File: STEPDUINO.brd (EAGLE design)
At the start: 112.4 x 73.7 mm, 126 parts, among them IC1 HEF4050B, IC2 MC34063, IC3 LD111733, IC4 74HC4094, IC5 ATmega32U4, IC6 DRV8811, IC7 DRV8811, J1 SERVO, J10 Touchscreen, J11 Touchscreen, J12 X-MOTOR, J13 MS1, J14 MS0, J15 Y-MOTOR, J16 MS1, J17 MS0, J2 Z-DRIVE, J3 ISP, J4 UART, J5 12V Supply, J6 MicroSD Card, J7 HWB, J8 USB-6PSMT, J9 Home Switches, Q1 16MHz

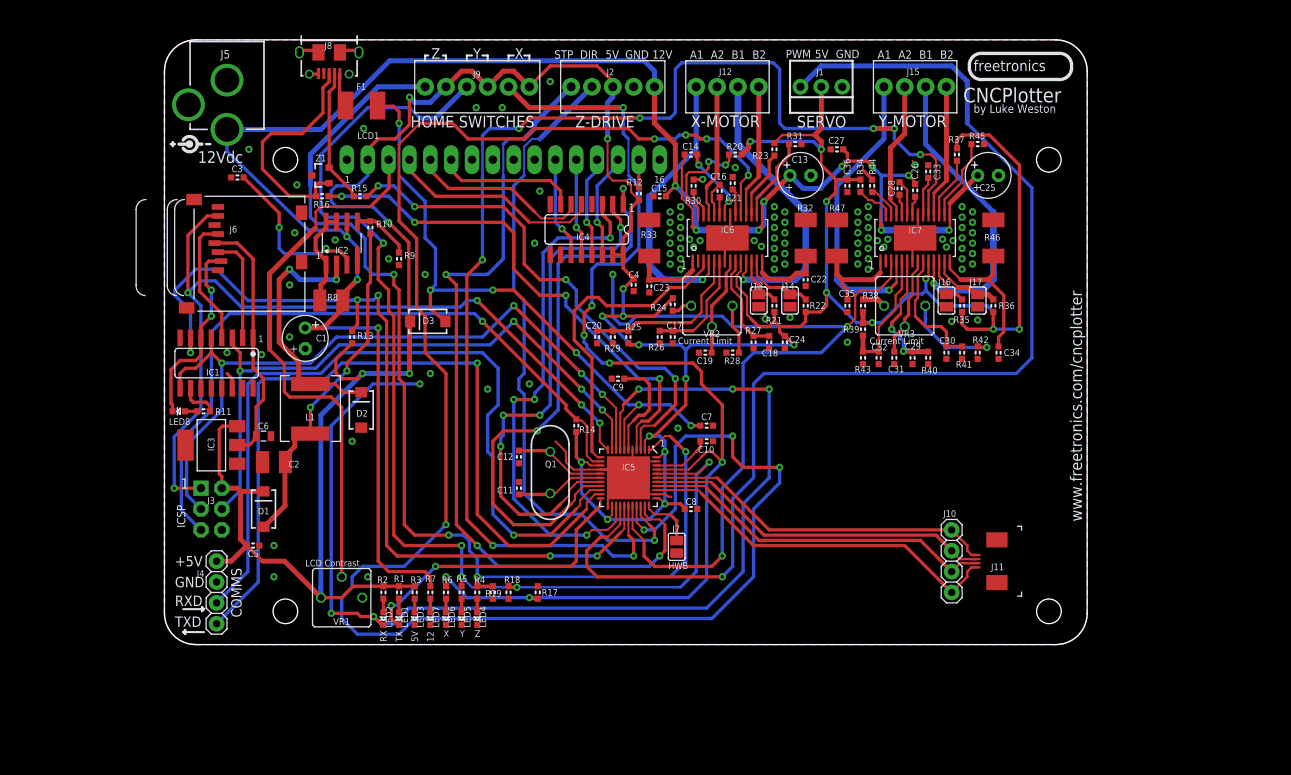
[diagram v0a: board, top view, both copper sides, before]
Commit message: Start of major restructure using ATmega328
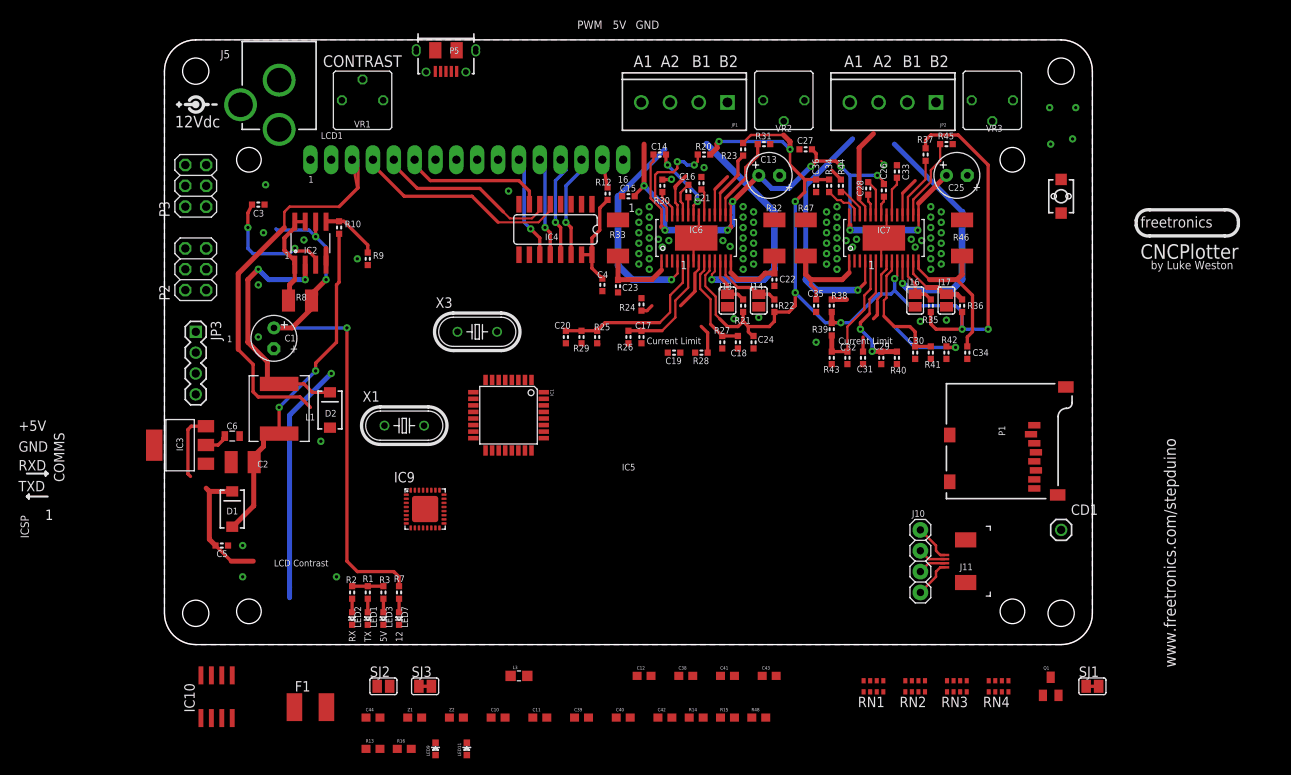
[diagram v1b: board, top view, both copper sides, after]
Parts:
- removed C7, C8: 100nF, freetronics-master-v1:0603
- removed C9: 1µF, freetronics-master-v1:0603
- removed D3: CDBA120, freetronics-luke:SMA
- removed IC5: ATmega32U4, freetronics-jon:QFN-44N
- removed J1: SERVO, con-molex:22-23-2031
- removed J12: X-MOTOR, con-phoenix-254:4POL254
- removed J15: Y-MOTOR, con-phoenix-254:4POL254
- removed J2: Z-DRIVE, con-phoenix-254:5POL254
- removed J3: ISP, SparkFun:2X3-NS
- removed J4: UART, pinhead:1X04
- removed J6: MicroSD Card, RAMPSdisplay:ADAFRUIT_MICROSD
- removed J7: HWB, freetronics-luke:SJ
- removed J8: USB-6PSMT, freetronics-jon:USB-MICROB-MB05PMXX
- removed J9: Home Switches, con-phoenix-254:6POL254
- removed LED4: Z, freetronics-master-v1:LED-0603
- removed LED5: Y, freetronics-master-v1:LED-0603
- removed LED6: X, freetronics-master-v1:LED-0603
- removed LED8: SD, freetronics-master-v1:LED-0603
- removed R11, R4, R5, R6: 1k, freetronics-master-v1:0603
- removed R17, R18, R19: 10k, freetronics-master-v1:0603
- added C38, C41, C43, C44: 100nF 0603, freetronics:0603
- added C39, C40: 22pF 0603, freetronics:0603
- added C42: 1uF 0603, freetronics:0603
- added CD1: M01PTH, freetronics-2:1X01
- added IC10: LM358D, linear:SO08
- added IC9: ATMEGA16U2-MU, freetronics-jon:ATMEL_QFN32
- added JP1, JP2: (no value), freetronics-master-v1:SCREWTERMINAL-3.5MM-4
- added JP3: (no value), freetronics-master-v1:1X04
- added L3: 0805 INDUCTOR, freetronics-master-v1:0805-LARGE
- added LED11: TX/YEL, freetronics:LED-0603
- added LED9: RX/GRN, freetronics:LED-0603
- added P1: microSD, freetronics-master-v1:MICRO-SD-SOCKET-PP
- added P2: ICSP:MAIN, pinhead:2X03
- added P3: ICSP:USB, pinhead:2X03
- added P5: USB-6PSMT, freetronics-jon:USB-MICROB-MB05PMXX
- added R48: 27R 0603, freetronics:0603
- added RN1: 2K2, freetronics-master-v1:CAY16
- added RN2, RN3: 1K, freetronics-master-v1:CAY16
- added RN4: 10K, freetronics-master-v1:CAY16
- added S7: RESET, freetronics-master-v1:TACTILE_SWITCH_SMD_2PIN_TINY
- added SJ1: GROUND, freetronics-jon:SJC
- added SJ2: UBOOT, jumper:SJ
- added SJ3: RESET-EN, freetronics-jon:SJC
- added X1, X3: 16MHz, freetronics-master-v1:HC49U-V
- added Z2: PGB1010603, freetronics:0603
- C10: value 100nF -> 22pF 0603; device freetronics-master-v1:0603 -> freetronics:0603
- C11: value 22pF -> 22pF 0603; device freetronics-master-v1:0603 -> freetronics:0603
- C12: value 22pF -> 100nF 0603; device freetronics-master-v1:0603 -> freetronics:0603
- F1: value 500mA -> 500mA PTC 1812; device freetronics-luke:1812 -> rcl:L1812
- IC1: value HEF4050B -> ATMEGA328P TQFP32; device 40xx:SO16 -> freetronics-2:TQFP32-08
- IC3: value LD111733 -> LD111733 SOT-223
- Q1: value 16MHz -> FDN340P; device freetronics-master-v1:HC49US -> freetronics-master-v1:SOT23
- R13: value 10k -> 1M 0603; device freetronics-master-v1:0603 -> freetronics:0603
- R14: value 10k -> 22R 0603; device freetronics-master-v1:0603 -> freetronics:0603
- R15: value 22R -> 22R 0603; device freetronics-master-v1:0603 -> freetronics:0603
- R16: value 22R -> 1M 0603; device freetronics-master-v1:0603 -> freetronics:0603
- Z1: value PGB102ST23 -> PGB1010603; device freetronics-luke:SOT23-3 -> freetronics:0603
- moved R15 77.7 mm to (68.6, -8.89), turned to 0 degrees
- moved F1 73.5 mm to (17.8, -7.62)
- moved R16 68.0 mm to (29.2, -12.7), turned to 0 degrees
- moved Z1 67.0 mm to (30.5, -8.89), turned to 0 degrees
- moved Q1 66.3 mm to (108.0, -5.08), turned to 0 degrees
- moved VR1 60.6 mm to (24.1, 66.3)
- moved R13 50.2 mm to (25.4, -12.7), turned to 0 degrees
- moved C10 42.2 mm to (40.6, -8.89), turned to 0 degrees
- moved R14 38.4 mm to (64.8, -8.89), turned to 0 degrees
- moved IC1 36.1 mm to (41.9, 27.9), turned to 270 degrees
- moved C12 30.7 mm to (58.4, -3.81), turned to 0 degrees
- moved C11 28.1 mm to (45.7, -8.89), turned to 0 degrees
- moved VR3 27.2 mm to (100.8, 66.3)
- moved VR2 26.5 mm to (75.4, 66.3)
- moved J5 6.35 mm to (14.0, 76.5)
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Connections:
- removed net !RESET: IC5.13, J3.5, R14.1
- removed net !SD_CS: IC1.7, IC5.27, R13.1
- removed net +5V: C24.1, C36.1, C4.1, C5.1, C8.2, D1.K, D3.K, IC3.3, IC4.15, IC4.16, IC5.14, IC5.2, IC5.24, IC5.34, IC5.44, IC6.10, IC7.10, J1.2, J2.3, J3.2, J4.1, J9.1, J9.3, J9.5, LCD1.2, R1.2, R12.2, R13.2, R14.2, R2.2, R20.2, R21.2, R22.2, R23.2, R24.2, R25.2, R3.2, R34.2, R35.2, R36.2, R37.2, R38.2, R39.2, VR1.A
- removed net FOO: IC1.6, J6.2, LED8.C
- removed net HWB: IC5.33, J7.2
- removed net LCD_CLOCK: IC4.3, IC5.25
- removed net LCD_DATA: IC4.2, IC5.18
- removed net LCD_STROBE: IC4.1, IC5.19
- removed net MISO: IC5.11, J3.1, J6.7
- removed net MOSI: IC1.3, IC5.10, J3.4
- removed net MOSI_3.3V: IC1.2, J6.3
- removed net N$12: LED4.A, R4.1
- removed net N$2: F1.1, J8.VBUS
- removed net N$33: J8.D+, R16.2, Z1.1
- removed net N$34: J8.D-, R15.2, Z1.2
- removed net N$35: C11.2, IC5.17, Q1.2
- removed net N$39: LED5.A, R5.1
- removed net N$41: LED6.A, R6.1
- removed net N$5: IC7.11, J15.3
- removed net RXD: IC5.20, J4.3
- removed net SCK: IC1.5, IC1.9, IC5.9, J3.3
- removed net SCK_3.3V: IC1.4, J6.5
- removed net SERVO: IC5.26, J1.3
- removed net TOUCH1: IC5.36, J10.1, J11.Y1
- removed net TOUCH2: IC5.37, J10.2, J11.X2
- removed net TOUCH3: IC5.38, J10.3, J11.Y2
- removed net TOUCH4: IC5.39, J10.4, J11.X1
- removed net TXD: IC5.21, J4.4
- removed net VDD: C6.1, IC1.1, IC3.2, J6.4
- removed net X_DIR: IC5.12, IC6.3
- removed net X_HOME: IC5.41, J9.2, R17.1, R6.2
- removed net X_STEP: IC5.30, IC6.19
- removed net Y_DIR: IC5.29, IC7.3
- removed net Y_HOME: IC5.40, J9.4, R18.1, R5.2
- removed net Y_STEP: IC5.28, IC7.19
- removed net Z_DIR: IC5.31, J2.4
- removed net Z_HOME: IC5.1, J9.6, R19.1, R4.2
- removed net Z_STEP: IC5.32, J2.5
- new net +3V3: C6.1, IC3.2
- new net 3V3D: C44.1, IC10.2, P1.4
- new net 5V: C12.1, C24.1, C36.1, C4.1, C41.1, C43.1, C5.1, D1.K, IC1.18, IC1.4, IC1.6, IC10.8, IC3.3, IC4.15, IC4.16, IC6.10, IC7.10, IC9.32, IC9.4, JP3.1, LCD1.2, LED11.A, LED9.A, P2.2, P3.2, Q1.2, R1.2, R12.2, R2.2, R20.2, R21.2, R22.2, R23.2, R24.2, R25.2, R3.2, R34.2, R35.2, R36.2, R37.2, R38.2, R39.2, RN4.7, RN4.8, VR1.A
- new net A0: IC1.23, J10.1, J11.Y1
- new net A1: IC1.24, J10.2, J11.X2
- new net A2: IC1.25, J10.3, J11.Y2
- new net A3: IC1.26, J10.4, J11.X1
- new net A4_SDA: IC1.27
- new net A5_SCL: IC1.28
- new net A6: IC1.19
- new net A7: IC1.22
- new net AREF: IC1.20
- new net D0_RX: IC1.30, JP3.2, RN3.4
- new net D10_SS: IC1.14
- new net D11_MOSI: IC1.15, P2.4, RN2.6
- new net D12_MISO: IC1.16, P1.7, P2.1
- new net D13_SCK: IC1.17, P2.3, RN2.7
- new net D1_TX: IC1.31, JP3.3, RN3.3
- new net D2: IC1.32, IC4.1
- new net D3: IC1.1, IC4.2
- new net D4: IC1.2, IC4.3
- new net D5: IC1.9, IC6.3
- new net D6: IC1.10, IC6.19
- new net D7: IC1.11, IC7.3
- new net D8: IC1.12, IC7.19
- new net D9: IC1.13, RN2.5
- new net DTR: IC9.13, SJ2.2, SJ3.1
- new net MISO2: IC9.17, P3.1
- new net MOSI2: IC9.16, P3.4
- new net N$113: C39.2, IC9.2, R16.2, X1.2
- new net N$114: C40.2, R16.1, R48.2, X1.1
- new net N$115: F1.1, P5.VBUS
- new net N$117: C42.1, IC9.27
- new net N$77: IC7.4, JP2.4
- new net N$81: IC10.1, IC10.5
- new net N$82: P1.2, RN1.8, RN2.4
- new net N$83: P1.3, RN1.6, RN2.3
- new net N$84: P1.5, RN1.7, RN2.2
- new net N$87: CD1.1, P1.CD1
- new net N$88: LED11.C, RN3.1
- new net N$89: LED9.C, RN3.2
- new net N$90: C38.1, SJ3.2
- new net RD+: IC9.29, R15.1
- new net RD-: IC9.30, R14.1
- new net RESET: C38.2, IC1.29, P2.5, RN4.2, S7.2
- new net RESET2: IC9.24, P3.5, RN4.1
- new net SCK2: IC9.15, P3.3
- new net USBGND: IC9.28, L3.2, P5.GND, SJ1.1
- new net USBRXD: IC9.9, RN3.5
- new net USBTXD: IC9.8, RN3.6
- new net USBVCC: F1.2, IC9.31, Q1.3
- net +12V: now also RN4.3; no longer J2.1
- net GND: now also C12.2, C39.1, C40.1, C41.2, C42.2, C43.2, C44.2, IC1.21, IC1.3, IC1.5, IC10.4, IC9.3, IC9.EXP, JP3.4, P1.6, P1.CD2, P1.GND1, P1.GND2, P2.6, P3.6, RN1.1, RN1.2, RN1.3, RN4.4, S7.1, SJ1.2, SJ2.1; no longer C12.1, C7.2, C8.1, C9.1, IC1.11, IC1.14, IC1.8, IC5.15, IC5.23, IC5.35, IC5.43, IC5.5, IC5.TGND, J1.1, J2.2, J3.6, J4.2, J6.6, J6.MT1, J6.MT2, J7.1, J8.FIX1, J8.FIX2, J8.GND, J8.PIN1, J8.PIN2, J8.TAB1, J8.TAB2, LED4.C, LED5.C, LED6.C, R17.2, R18.2, R19.2, Z1.3
- net N$1: now also IC7.11, JP2.2; no longer IC7.4, J15.1
- net N$11: now also IC1.7, R13.2, X3.2; no longer IC5.42
- net N$21: now also JP1.1; no longer J12.4
- net N$22: now also JP1.2; no longer J12.3
- net N$23: now also JP1.3; no longer J12.2
- net N$28: now also C11.2, IC1.8, R13.1, X3.1; no longer C9.2, IC5.6
- net N$3: now also JP1.4; no longer J12.1
- net N$36: now also IC9.1, R48.1; no longer C12.2, IC5.16, Q1.1
- net N$37: now also L3.1, P5.FIX1, P5.FIX2, P5.PIN1, P5.PIN2, P5.TAB1, P5.TAB2, Z1.2, Z2.2; no longer IC5.4, R16.1
- net N$38: now also P5.D+, R15.2, Z1.1; no longer IC5.3, R15.1
- net N$4: now also JP2.1; no longer J15.4
- net N$40: now also P5.D-, R14.2, Z2.1; no longer C7.1, D3.A, F1.2, IC5.7
- net N$6: now also JP2.3; no longer J15.2
- net N$62: now also IC10.3, RN4.5, RN4.6; no longer LED8.A, R11.1
- net N$63: now also IC10.6, IC10.7, Q1.1; no longer IC1.10, R11.2
- net RXLED: now also IC9.10, RN3.7; no longer IC5.8
- net TXLED: now also IC9.11, RN3.8; no longer IC5.22
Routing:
- net +5V: track 445.8 -> 0.00 mm, vias 24 -> 0
- net X_STEP: track 222.4 -> 0.00 mm, vias 8 -> 0
- net 5V: track 0.00 -> 208.9 mm, vias 0 -> 9
- net Y_STEP: track 154.8 -> 0.00 mm, vias 8 -> 0
- net SERVO: track 146.0 -> 0.00 mm, vias 1 -> 0
- net Y_HOME: track 140.9 -> 0.00 mm, vias 5 -> 0
- net RXLED: track 138.4 -> 0.00 mm, vias 6 -> 0
- net X_HOME: track 138.1 -> 0.00 mm, vias 7 -> 0
- net Z_HOME: track 133.1 -> 0.00 mm, vias 4 -> 0
- net !SD_CS: track 106.9 -> 0.00 mm, vias 5 -> 0
- net MISO: track 102.9 -> 0.00 mm, vias 5 -> 0
- net Y_DIR: track 102.9 -> 0.00 mm, vias 3 -> 0
- net Z_STEP: track 101.7 -> 0.00 mm, vias 3 -> 0
- net TXD: track 97.1 -> 0.00 mm, vias 1 -> 0
- net RXD: track 96.5 -> 0.00 mm, vias 1 -> 0
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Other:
- board size 112.4 x 73.7 mm -> 113 x 73.7 mm
- board text added: "(C) 2013 Freetronics Pty Ltd"
- board text added: "CONTRAST"
- board text added: "SKU: STEPDUINO"
- board text added: "StepDuino"
- board text added: "www.freetronics.com/stepduino"
- board text removed: "(C) 2012 Luke Weston"
- board text removed: "12V"
- board text removed: "CNC Plotter Controller"
- board text removed: "DIR"
- board text removed: "HOME SWITCHES"
- board text removed: "HWB"
- board text removed: "SKU: CNCPLOT"
- board text removed: "STP"
- board text removed: "X"
- board text removed: "Y"
- board text removed: "Z"
- board text removed: "www.freetronics.com/cncplotter"

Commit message: Routing for v1.0 release
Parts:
- removed C13, C25: 100uF, rcl:E2,5-6
- removed IC10: LM358D, linear:SO08
- removed IC9: ATMEGA16U2-MU, freetronics-jon:ATMEL_QFN32
- removed J10: Touchscreen, pinhead:1X04
- removed J13, J16: MS1, freetronics-luke:SJ
- removed J14, J17: MS0, freetronics-luke:SJ
- removed L3: 0805 INDUCTOR, freetronics-master-v1:0805-LARGE
- removed LED11: TX/YEL, freetronics:LED-0603
- removed LED7: 12, freetronics-master-v1:LED-0603
- removed LED9: RX/GRN, freetronics:LED-0603
- removed P5: USB-6PSMT, freetronics-jon:USB-MICROB-MB05PMXX
- removed RN3: 1K, freetronics-master-v1:CAY16
- removed RN4: 10K, freetronics-master-v1:CAY16
- removed S7: RESET, freetronics-master-v1:TACTILE_SWITCH_SMD_2PIN_TINY
- removed X1, X3: 16MHz, freetronics-master-v1:HC49U-V
- added C7, C8: 100uF 25V, rcl:PANASONIC_D
- added IC5: DRV8811, eje-components:HTSSOP28
- added IC8: LM358D, linear:SO08
- added J2: Touchscreen, pinhead:1X04
- added JP4: Servo1, freetronics-master-v1.1:1X03
- added JP5: Servo2, freetronics-master-v1.1:1X03
- added JP6: I2C, freetronics-master-v1:1X04
- added JP7: (no value), freetronics-master-v1.1:1X02
- added L2: 0805 INDUCTOR, freetronics-master-v1:0805-LARGE
- added LED4: GREEN 0603, freetronics-master-v1:LED-0603
- added P4: USB-6PSMT, freetronics-jon:USB-MICROB-MB05PMXX
- added R11, R17, R18, R4, R5, R6: 10K 0603, freetronics:0603@1
- added R19, R49: 4K7 0603, freetronics:0603@1
- added SJ4, SJ6: MS1, freetronics-luke:SJ
- added SJ5, SJ7: MS0, freetronics-luke:SJ
- added SW1: RESET, freetronics-master-v1:TACTILE_SWITCH_SMD_2PIN_TINY
- added XTL1, XTL2: 16MHz, freetronics-master-v1:HC49U-V
- C1: value 100uF -> 100uF 25V; device rcl:E2,5-6 -> rcl:PANASONIC_D
- C14, C16: value 220nF -> 220nF 0603
- C15, C5: value 100nF -> 100nF 0603
- C2: value 47µF -> 47uF 10V 1210
- C3: value 100pF -> 100pF 0603
- C6: value 10µF -> 10uF 10V 0805
- IC7: value DRV8811 -> ATMEGA16U2-MU; device eje-components:HTSSOP28 -> freetronics-jon:ATMEL_QFN32
- JP3: value (none) -> SERIAL
- LED1: value TX -> GREEN/TX 0603
- LED2: value RX -> YELLOW/RX 0603
- LED3: value 5V -> BLUE/5V 0603
- R1, R2: value 1k -> 1K 0603
- R10: value 3k0 -> 3k0 0603
- R3: value 1k -> 1K8 0603
- R32, R33, R46, R47: value 0.20Ω 1W -> 0.2R 1W
- R7: value 4k7 -> 3K9 0603
- R8: value 0.2Ω -> 0.2R 0.5W 1210
- R9: value 1k -> 1k 0603
- VR1, VR2, VR3: value 10kΩ -> 10K
- moved P3 105.5 mm to (109.2, 59.7), turned to 270 degrees
- moved P2 105.4 mm to (109.2, 48.3), turned to 270 degrees
- moved SJ1 97.8 mm to (16.0, 7.11)
- moved Q1 83.7 mm to (30.2, 25.9), turned to 180 degrees
- moved C5 81.7 mm to (87.1, 28.2), turned to 90 degrees
- moved IC3 80.9 mm to (82.5, 30.5), turned to 0 degrees
- moved C6 74.3 mm to (82.5, 23.4), turned to 270 degrees
- moved IC7 69.7 mm to (26.2, 16.8), turned to 90 degrees
- moved C44 68.1 mm to (85.3, 23.4), turned to 270 degrees
- moved C1 64.7 mm to (74.7, 57.9)
- moved R15 64.5 mm to (8.38, 14.2), turned to 180 degrees
- moved LED3 62.0 mm to (4.95, 61.2), turned to 180 degrees
- moved R14 61.7 mm to (8.38, 16.3), turned to 180 degrees
- moved LED2 56.4 mm to (4.95, 56.6), turned to 180 degrees
- moved LED1 55.4 mm to (4.95, 54.9), turned to 180 degrees
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- renumbered J11 to J3, J5 to J1
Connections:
- removed net 3V3D: C44.1, IC10.2, P1.4
- removed net N$88: LED11.C, RN3.1
- removed net N$89: LED9.C, RN3.2
- net +12V: now also C7.+, C8.+, IC5.15, IC5.28, R6.2; no longer C13.+, C25.+, IC7.15, IC7.28, RN4.3
- net +3V3: now also C44.1, IC8.2, P1.4
- net 5V: now also IC5.10, IC7.32, IC7.4, IC8.8, JP4.2, JP5.2, JP6.1, R19.2, R4.2, R49.2, R5.2; no longer IC10.8, IC7.10, IC9.32, IC9.4, LED11.A, LED9.A, RN4.7, RN4.8
- net A0: now also J2.1; no longer J10.1
- net A1: now also J2.2; no longer J10.2
- net A2: now also J2.3; no longer J10.3
- net A3: now also J2.4; no longer J10.4
- net A4_SDA: now also JP6.2, R19.1
- net A5_SCL: now also JP6.3, R49.1
- net A6: now also JP7.1
- net A7: now also JP7.2
- net D0_RX: now also R18.1; no longer RN3.4
- net D10_SS: now also JP4.1
- net D11_MOSI: now also JP5.1
- net D1_TX: now also R17.1; no longer RN3.3
- net D2: now also IC5.3; no longer IC4.1
- net D3: now also IC6.3; no longer IC4.2
- net D4: now also IC4.1; no longer IC4.3
- net D5: now also IC5.19; no longer IC6.3
- net D7: now also IC4.2; no longer IC7.3
- net D8: now also IC4.3; no longer IC7.19
- net DTR: now also IC7.13; no longer IC9.13
- net GND: now also C7.-, C8.-, IC5.21, IC5.7, IC5.P$1, IC7.3, IC7.EXP, IC8.4, JP4.3, JP5.3, JP6.4, LED4.C, R11.1, SJ4.1, SJ5.1, SJ6.1, SJ7.1, SW1.1; no longer C13.-, C25.-, IC10.4, IC7.21, IC7.7, IC7.P$1, IC9.3, IC9.EXP, J13.1, J14.1, J16.1, J17.1, LED7.C, RN4.4, S7.1
- net MISO2: now also IC7.17; no longer IC9.17
- net MOSI2: now also IC7.16; no longer IC9.16
- net N$1: now also IC6.11; no longer IC7.11
- net N$10: now also IC6.20; no longer IC7.20
- net N$11: now also XTL2.2; no longer X3.2
- net N$113: now also IC7.2, XTL1.2; no longer IC9.2, X1.2
- net N$114: now also XTL1.1; no longer X1.1
- net N$115: now also P4.VBUS; no longer P5.VBUS
- net N$117: now also IC7.27; no longer IC9.27
- net N$13: now also IC6.1; no longer IC7.1
- net N$14: now also IC6.14; no longer IC7.14
- net N$15: now also IC6.5; no longer IC7.5
- net N$16: now also IC6.6; no longer IC7.6
- net N$17: now also IC5.24; no longer IC6.24
- net N$18: now also IC5.23; no longer IC6.23
- net N$19: now also IC5.16; no longer IC6.16
- net N$20: now also IC6.9; no longer IC7.9
- net N$21: now also IC5.18; no longer IC6.18
- net N$22: now also IC5.11; no longer IC6.11
- net N$23: now also IC5.25; no longer IC6.25
- net N$24: now also IC5.22; no longer IC6.22
- net N$25: now also IC5.5; no longer IC6.5
- net N$26: now also IC5.20; no longer IC6.20
- net N$27: now also IC5.6; no longer IC6.6
- net N$28: now also XTL2.1; no longer X3.1
- net N$3: now also IC5.4; no longer IC6.4
- net N$36: now also IC7.1; no longer IC9.1
- net N$37: now also L2.1, P4.FIX1, P4.FIX2, P4.PIN1, P4.PIN2, P4.TAB1, P4.TAB2; no longer L3.1, P5.FIX1, P5.FIX2, P5.PIN1, P5.PIN2, P5.TAB1, P5.TAB2
- net N$38: now also P4.D+; no longer P5.D+
- net N$4: now also IC6.18; no longer IC7.18
- net N$40: now also P4.D-; no longer P5.D-
- net N$42: now also LED4.A; no longer LED7.A
- net N$46: now also IC5.1; no longer IC6.1
- net N$47: now also IC5.14; no longer IC6.14
- net N$48: now also IC5.9; no longer IC6.9
- net N$49: now also IC5.27; no longer IC6.27
- net N$57: now also IC5.17; no longer IC6.17
- net N$6: now also IC6.25; no longer IC7.25
- net N$62: now also IC8.3, R11.2, R6.1; no longer IC10.3, RN4.5, RN4.6
- net N$63: now also IC8.6, IC8.7; no longer IC10.6, IC10.7
- net N$64: now also IC5.8; no longer IC6.8
- net N$65: now also IC5.26; no longer IC6.26
- net N$66: now also IC5.12, SJ4.2; no longer IC6.12, J13.2
- net N$67: now also IC5.13, SJ5.2; no longer IC6.13, J14.2
- net N$68: now also IC6.27; no longer IC7.27
- net N$69: now also IC6.17; no longer IC7.17
- net N$7: now also IC6.24; no longer IC7.24
- net N$72: now also IC6.8; no longer IC7.8
- net N$73: now also IC6.26; no longer IC7.26
- net N$74: now also IC6.12, SJ6.2; no longer IC7.12, J16.2
- net N$75: now also IC6.13, SJ7.2; no longer IC7.13, J17.2
- net N$76: now also IC6.16; no longer IC7.16
- net N$77: now also IC6.4; no longer IC7.4
- net N$8: now also IC6.23; no longer IC7.23
- net N$81: now also IC8.1, IC8.5; no longer IC10.1, IC10.5
- net N$82: now also RN1.6; no longer RN1.8
- net N$83: now also RN1.7; no longer RN1.6
- net N$84: now also RN1.8; no longer RN1.7
- net N$9: now also IC6.22; no longer IC7.22
- net RD+: now also IC7.29; no longer IC9.29
- net RD-: now also IC7.30; no longer IC9.30
- net RESET: now also R5.1, SW1.2; no longer RN4.2, S7.2
- net RESET2: now also IC7.24, R4.1; no longer IC9.24, RN4.1
- net RXLED: now also IC7.10; no longer IC9.10, RN3.7
- net SCK2: now also IC7.15; no longer IC9.15
- net TXLED: now also IC7.11; no longer IC9.11, RN3.8
- net USBGND: now also IC7.28, L2.2, P4.GND; no longer IC9.28, L3.2, P5.GND
- net USBRXD: now also IC7.9, R18.2; no longer IC9.9, RN3.5
- net USBTXD: now also IC7.8, R17.2; no longer IC9.8, RN3.6
- net USBVCC: now also IC7.31; no longer IC9.31
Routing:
- net 5V: track 208.9 -> 477.6 mm, vias 9 -> 15
- net D11_MOSI: track 0.00 -> 176.7 mm, vias 0 -> 3
- net RESET2: track 0.00 -> 114.2 mm, vias 0 -> 1
- net MOSI2: track 0.00 -> 111.7 mm, vias 0 -> 1
- net MISO2: track 0.00 -> 110.0 mm, vias 0 -> 1
- net SCK2: track 0.00 -> 107.8 mm, vias 0 -> 1
- net A4_SDA: track 0.00 -> 106.4 mm, vias 0 -> 2
- net D6: track 0.00 -> 103.3 mm, vias 0 -> 2
- net D0_RX: track 0.00 -> 102.4 mm, vias 0 -> 2
- net A5_SCL: track 0.00 -> 100.7 mm, vias 0 -> 2
- net D1_TX: track 0.00 -> 96.5 mm, vias 0 -> 2
- net D13_SCK: track 0.00 -> 93.7 mm, vias 0 -> 2
- net D12_MISO: track 0.00 -> 93.0 mm, vias 0 -> 3
- net D5: track 0.00 -> 91.6 mm, vias 0 -> 2
- net D2: track 0.00 -> 87.8 mm, vias 0 -> 2
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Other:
- board text added: "12"
- board text added: "16U2"
- board text added: "328P"
- board text added: "A"
- board text added: "A0"
- board text added: "A0: Touch 1 A1: Touch 2 A2: Touch 3 A3: Touch 4 A4: SDA / Spare A5: SCL / Spare A6: Spare A7: Spare"
- board text added: "A3"
- board text added: "A4"
- board text added: "A5"
- board text added: "A6"
- board text added: "A7"
- board text added: "D0: RX D1: TX D2: Stepper 1 Direction D3: Stepper 2 Direction D4: LCD Strobe D5: Stepper 1 Step D6: Stepper 2 Step D7: LCD Data D8: LCD Clock D9: uSD nCS D10: SPI SS D11: SPI MOSI D12: SPI MISO D13: SPI SCK"
- board text added: "D10"
- board text added: "D11"
- board text added: "I2C"
- board text added: "K"
- board text added: "MAX CURRENT"
- board text added: "RX"
- board text added: "SERVO1"
- board text added: "SERVO2"
- board text added: "STEPPER 1"
- board text added: "STEPPER 2"
- board text added: "SW1"
- board text added: "StepDuino Stepper Motor Controller"
- board text added: "TOUCH"
- board text added: "TX"
- board text added: "UART"
- board text added: "v1.0"
- board text removed: "CNCPlotter"
- board text removed: "COMMS"
- board text removed: "Current Limit"
- board text removed: "IC5"
- board text removed: "J5"
- board text removed: "LCD Contrast"
- board text removed: "PWM"
- board text removed: "RXD"
- board text removed: "TXD"
- board text removed: "V1.0"
- board text removed: "by Luke Weston"

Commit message: Added documentation and preview image
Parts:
- removed C43, C44: 100nF 0603, freetronics:0603
- removed J3: Touchscreen, SparkFun:DS_TOUCH_CONNECTOR
- added C25: 220nF, freetronics-master-v1:0603
- added C37: 22pF 0603, freetronics:0603
- added C9: 100nF 0603, freetronics:0603@1
- C1, C8: value 100uF 25V -> 100uF 50V; device rcl:PANASONIC_D -> freetronics-original:PANASONIC_E
- C26, C33: value 220nF -> 100nF
- C27, C32: value 100nF -> 220nF
- C28: value 220nF -> 1nF
- C30: value 1nF -> 100nF
- C36: value 100nF -> 100nF 0603; device freetronics-master-v1:0603 -> freetronics:0603
- C38: value 100nF 0603 -> 22pF 0603
- C39: value 22pF 0603 -> 100nF 0603
- C40: value 22pF 0603 -> 1uF 0603
- C42: value 1uF 0603 -> 100nF 0603
- C7: device rcl:PANASONIC_D -> freetronics-original:PANASONIC_E
- moved C42 64.3 mm to (85.3, 23.4), turned to 270 degrees
- moved C38 56.2 mm to (23.1, 4.32), turned to 180 degrees
- moved C36 27.1 mm to (78.5, 14.0)
- moved C32 20.5 mm to (85.9, 60.2), turned to 90 degrees
- moved C34 19.0 mm to (78.1, 43.7)
- moved C33 18.3 mm to (97.2, 43.7), turned to 270 degrees
- moved C40 18.1 mm to (21.1, 22.4), turned to 90 degrees
- moved C39 18.1 mm to (25.7, 22.4), turned to 270 degrees
- moved C35 16.4 mm to (93.0, 36.8)
- moved C28 15.7 mm to (86.4, 39.9)
- moved C41 11.6 mm to (35.6, 28.4)
- moved C7 7.77 mm to (24.4, 50.0)
- moved C26 7.04 mm to (81.7, 59.1), turned to 180 degrees
- moved C27 6.27 mm to (85.7, 55.6), turned to 270 degrees
- moved C31 5.08 mm to (83.3, 39.9)
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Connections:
- net +12V: now also C25.1; no longer C27.1
- net +3V3: now also C42.1; no longer C44.1
- net 5V: now also C35.1, C39.1; no longer C36.1, C43.1
- net A0: no longer J3.Y1
- net A1: no longer J3.X2
- net A2: no longer J3.Y2
- net A3: no longer J3.X1
- net AREF: now also C9.1
- net GND: now also C26.2, C28.2, C37.1, C38.1, C39.2, C40.2, C9.2; no longer C27.2, C36.2, C39.1, C40.1, C43.2, C44.2
- net N$10: now also C32.1; no longer C33.1
- net N$113: now also C37.2; no longer C39.2
- net N$114: now also C38.2; no longer C40.2
- net N$117: now also C40.1; no longer C42.1
- net N$13: now also C34.1; no longer C35.1
- net N$14: now also C33.1; no longer C34.1
- net N$15: now also C31.1; no longer C32.1
- net N$16: now also C28.1; no longer C29.1
- net N$20: now also C29.1; no longer C30.1
- net N$7: now also C27.2; no longer C28.2
- net N$72: now also C30.1; no longer C31.1
- net N$8: now also C27.1; no longer C28.1
- net N$9: now also C25.2; no longer C26.2
- net N$90: now also C36.1; no longer C38.1
- net RESET: now also C36.2; no longer C38.2
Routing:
- net A0: track 42.0 -> 56.0 mm
- net A1: track 39.0 -> 50.6 mm
- net N$9: track 2.37 -> 14.0 mm, vias 0 -> 2
- net 5V: track 477.6 -> 471.0 mm
- net A2: track 38.6 -> 45.2 mm
- net N$29: track 23.5 -> 18.1 mm
- net AREF: track 0.00 -> 5.09 mm
- net +12V: track 181.0 -> 183.4 mm, vias 9 -> 7
- net N$4: track 16.5 -> 18.6 mm
- net A6: track 77.2 -> 75.9 mm
- net RD-: track 14.7 -> 13.5 mm
- net N$115: track 15.7 -> 14.5 mm
- net RD+: track 16.7 -> 15.5 mm
- net N$10: track 7.05 -> 8.25 mm
- net N$47: track 9.66 -> 8.65 mm
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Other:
- board text added: "4K7 I2C PULLUPS"
- board text added: "A0: Spare A1: Spare A2: Spare A3: Spare A4: SDA / Spare A5: SCL / Spare A6: Spare A7: Spare"
- board text added: "CD"
- board text added: "D0"
- board text added: "D1"
- board text added: "MICROSTEP"
- board text added: "MS0"
- board text added: "MS1"
- board text added: "RESET"
- board text added: "RESET-EN"
- board text added: "SCL"
- board text added: "SDA"
- board text added: "SKU: STEPD"
- board text added: "Select "Arduino Uno" in the IDE"
- board text added: "UBOOT"
- board text added: "UGND"
- board text added: "v1.1"
- board text removed: "A0: Touch 1 A1: Touch 2 A2: Touch 3 A3: Touch 4 A4: SDA / Spare A5: SCL / Spare A6: Spare A7: Spare"
- board text removed: "SKU: STEPDUINO"
- board text removed: "TOUCH"
- board text removed: "v1.0"
